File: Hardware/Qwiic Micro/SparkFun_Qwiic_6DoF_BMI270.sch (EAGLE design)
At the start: 29 parts, among them J1 QWIIC_RIGHT_ANGLE, U1 BMI270

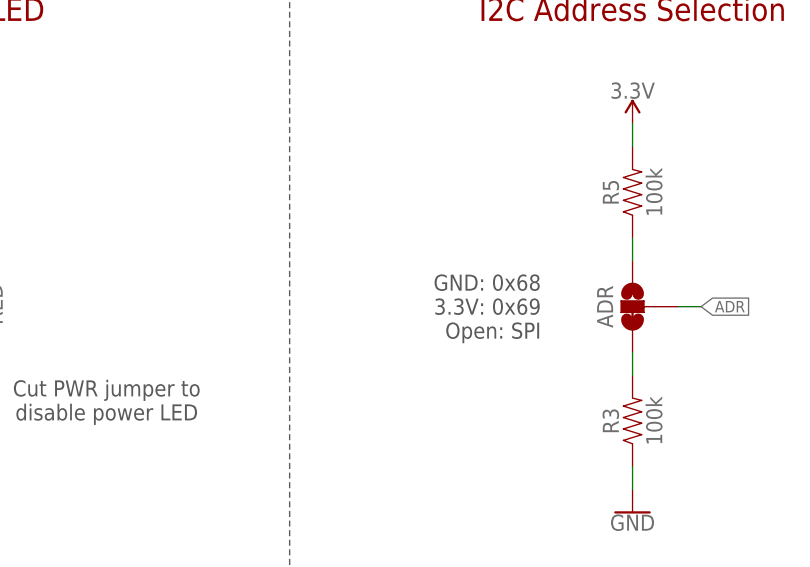
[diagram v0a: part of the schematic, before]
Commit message: Add "default" to I2C address in schematics
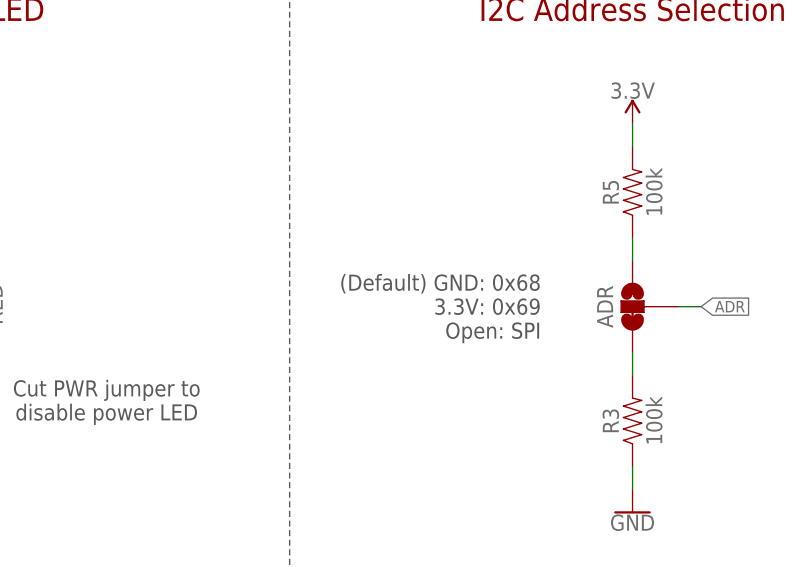
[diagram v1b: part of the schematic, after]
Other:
- note added: "(Default) GND: 0x68 3.3V: 0x69 Open: SPI"
- note removed: "GND: 0x68 3.3V: 0x69 Open: SPI"
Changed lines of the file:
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@@
 <sheet>
 <plain>
-<text x="101.6" y="30.48" size="1.778" layer="97" font="vector" align="center-right">GND: 0x68
+<text x="101.6" y="30.48" size="1.778" layer="97" font="vector" align="center-right">(Default) GND: 0x68
 3.3V: 0x69
 Open: SPI</text>
